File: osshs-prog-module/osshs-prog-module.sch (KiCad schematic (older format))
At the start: 13 parts, among them J1 Conn_02x03_Odd_Even, J2 Conn_01x04, J3 Conn_01x02, SW1 SW_Push, U1 STM32F103RETx

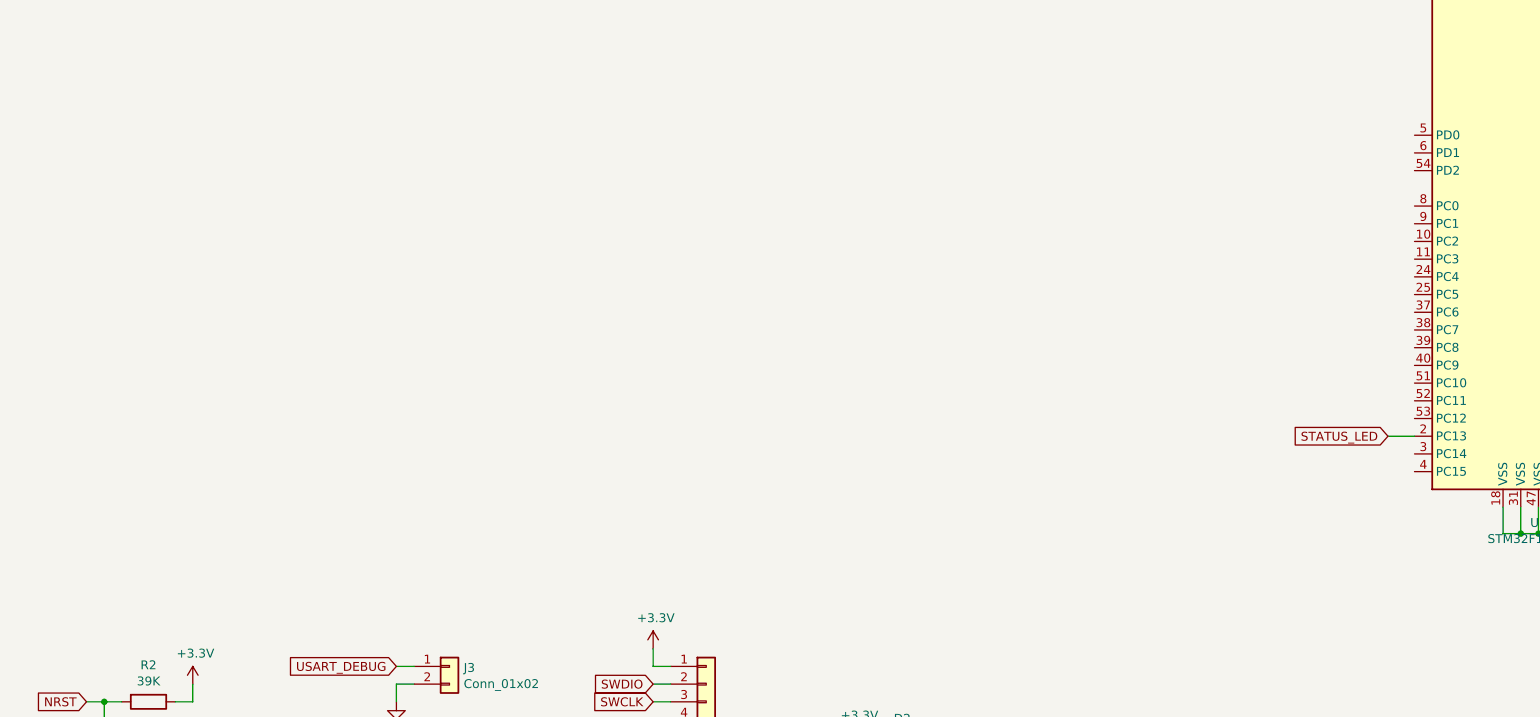
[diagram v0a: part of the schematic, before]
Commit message: Add CAN circuitry
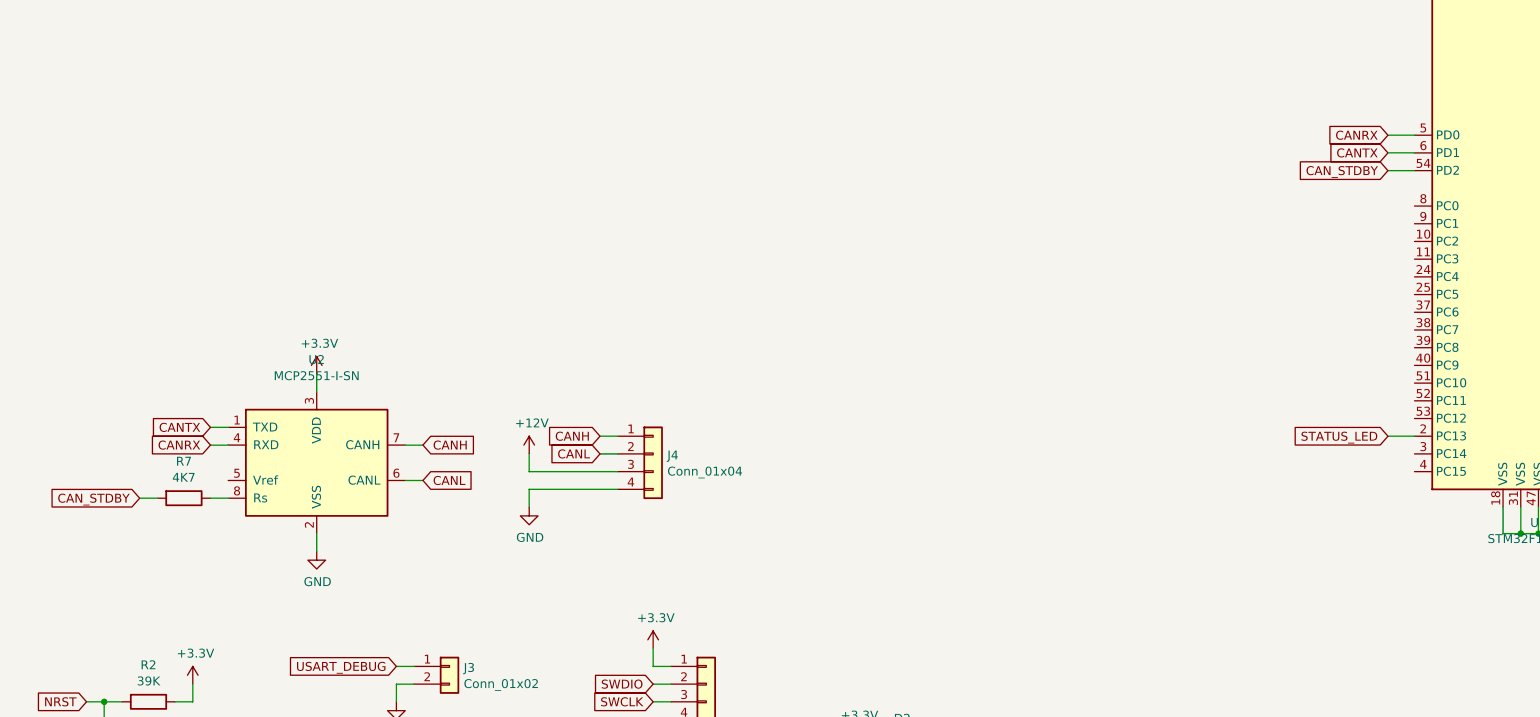
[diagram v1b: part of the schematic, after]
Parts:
- added J4: Conn_01x04, TerminalBlock:TerminalBlock_bornier-4_P5.08mm, symbol Connector_Generic:Conn_01x04
- added R7: 4K7, Resistor_SMD:R_0805_2012Metric, symbol Device:R
- added U2: MCP2551-I-SN, Package_SO:SOIC-8_3.9x4.9mm_P1.27mm, symbol Interface_CAN_LIN:MCP2551-I-SN
- J3: footprint (none) -> Connector_PinHeader_2.54mm:PinHeader_1x02_P2.54mm_Vertical
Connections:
- net +3V3: now also U2.3 (VDD)
- net GND: now also J4.4 (Pin_4), U2.2 (VSS)
- net CANRX: now reaches U1.5 (PD0)
- net CANRX: now also U2.4 (RXD)
- net CAN_STDBY: now reaches U1.54 (PD2)
- net CAN_STDBY: now also R7.2
- net CANTX: now reaches U1.6 (PD1)
- net CANTX: now also U2.1 (TXD)
- new net: R7.1, U2.8 (Rs)
- new net +12V: J4.3 (Pin_3)
- new net CANH: J4.1 (Pin_1), U2.7 (CANH)
- new net CANL: J4.2 (Pin_2), U2.6 (CANL)
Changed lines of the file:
@@
 F 0 "J3" H 2930 6092 50  0000 L CNN
 F 1 "Conn_01x02" H 2930 6001 50  0000 L CNN
-F 2 "" H 2850 6100 50  0001 C CNN
+F 2 "Connector_PinHeader_2.54mm:PinHeader_1x02_P2.54mm_Vertical" H 2850 6100 50  0001 C CNN
 F 3 "~" H 2850 6100 50  0001 C CNN
 	1    2850 6100
@@
 USART_DEBUG
 $Comp
-L power:GND #PWR?
+L power:GND #PWR0113
 U 1 1 5E18289F
 P 2550 6300
-F 0 "#PWR?" H 2550 6050 50  0001 C CNN
+F 0 "#PWR0113" H 2550 6050 50  0001 C CNN
 F 1 "GND" H 2555 6127 50  0000 C CNN
 F 2 "" H 2550 6300 50  0001 C CNN
@@
 Text GLabel 9850 2700 2    50   Input ~ 0
 USART_DEBUG
+$Comp
+L Interface_CAN_LIN:MCP2551-I-SN U2
+U 1 1 5E1DA5F9
+P 2100 4950
+F 0 "U2" H 2100 5531 50  0000 C CNN
+F 1 "MCP2551-I-SN" H 2100 5440 50  0000 C CNN
+F 2 "Package_SO:SOIC-8_3.9x4.9mm_P1.27mm" H 2100 4450 50  0001 C CIN
+F 3 "http://ww1.microchip.com/downloads/en/devicedoc/21667d.pdf" H 2100 4950 50  0001 C CNN
+	1    2100 4950
+	1    0    0    -1
+$EndComp
+Wire Wire Line
+	1600 5150 1500 5150
+$Comp
+L Device:R R7
+U 1 1 5E1E74DD
+P 1350 5150
+F 0 "R7" V 1143 5150 50  0000 C CNN
+F 1 "4K7" V 1234 5150 50  0000 C CNN
+F 2 "Resistor_SMD:R_0805_2012Metric" V 1280 5150 50  0001 C CNN
+F 3 "~" H 1350 5150 50  0001 C CNN
+	1    1350 5150
+	0    1    1    0
+$EndComp
+Wire Wire Line
+	2600 4850 2700 4850
+Wire Wire Line
+	2600 5050 2700 5050
+Text GLabel 2700 4850 2    50   Input ~ 0
+CANH
+Text GLabel 2700 5050 2    50   Input ~ 0
+CANL
+Wire Wire Line
+	2100 4550 2100 4450
+Wire Wire Line
+	2100 5350 2100 5450
+$Comp
+L power:GND #PWR0114
+U 1 1 5E1F498D
+P 2100 5450
+F 0 "#PWR0114" H 2100 5200 50  0001 C CNN
+F 1 "GND" H 2105 5277 50  0000 C CNN
+F 2 "" H 2100 5450 50  0001 C CNN
+F 3 "" H 2100 5450 50  0001 C CNN
+	1    2100 5450
+	1    0    0    -1
+$EndComp
+$Comp
+L power:+3.3V #PWR0115
+U 1 1 5E1F940E
+P 2100 4450
+F 0 "#PWR0115" H 2100 4300 50  0001 C CNN
+F 1 "+3.3V" H 2115 4623 50  0000 C CNN
+F 2 "" H 2100 4450 50  0001 C CNN
+F 3 "" H 2100 4450 50  0001 C CNN
+	1    2100 4450
+	1    0    0    -1
+$EndComp
+Wire Wire Line
+	1600 4750 1500 4750
+Wire Wire Line
+	1600 4850 1500 4850
+Text GLabel 1500 4750 0    50   Input ~ 0
+CANTX
+Text GLabel 1500 4850 0    50   Input ~ 0
+CANRX
+$Comp
+L Connector_Generic:Conn_01x04 J4
+U 1 1 5E20EEC2
+P 4000 4900
+F 0 "J4" H 4080 4892 50  0000 L CNN
+F 1 "Conn_01x04" H 4080 4801 50  0000 L CNN
+F 2 "TerminalBlock:TerminalBlock_bornier-4_P5.08mm" H 4000 4900 50  0001 C CNN
+F 3 "~" H 4000 4900 50  0001 C CNN
+	1    4000 4900
+	1    0    0    -1
+$EndComp
+Wire Wire Line
+	3800 4800 3700 4800
+Wire Wire Line
+	3800 4900 3700 4900
+Text GLabel 3700 4800 0    50   Input ~ 0
+CANH
+Text GLabel 3700 4900 0    50   Input ~ 0
+CANL
+Wire Wire Line
+	3800 5000 3300 5000
+Wire Wire Line
+	3300 5000 3300 4900
+Wire Wire Line
+	3300 5100 3300 5200
+Wire Wire Line
+	3300 5100 3800 5100
+$Comp
+L power:GND #PWR0116
+U 1 1 5E226228
+P 3300 5200
+F 0 "#PWR0116" H 3300 4950 50  0001 C CNN
+F 1 "GND" H 3305 5027 50  0000 C CNN
+F 2 "" H 3300 5200 50  0001 C CNN
+F 3 "" H 3300 5200 50  0001 C CNN
+	1    3300 5200
+	1    0    0    -1
+$EndComp
+$Comp
+L power:+12V #PWR0117
+U 1 1 5E228C10
+P 3300 4900
+F 0 "#PWR0117" H 3300 4750 50  0001 C CNN
+F 1 "+12V" H 3315 5073 50  0000 C CNN
+F 2 "" H 3300 4900 50  0001 C CNN
+F 3 "" H 3300 4900 50  0001 C CNN
+	1    3300 4900
+	1    0    0    -1
+$EndComp
+Wire Wire Line
+	8300 3100 8150 3100
+Text GLabel 8150 3100 0    50   Input ~ 0
+CANRX
+Wire Wire Line
+	8300 3200 8150 3200
+Text GLabel 8150 3200 0    50   Input ~ 0
+CANTX
+Wire Wire Line
+	1200 5150 1100 5150
+Text GLabel 1100 5150 0    50   Input ~ 0
+CAN_STDBY
+Wire Wire Line
+	8300 3300 8150 3300
+Text GLabel 8150 3300 0    50   Input ~ 0
+CAN_STDBY
 $EndSCHEMATC

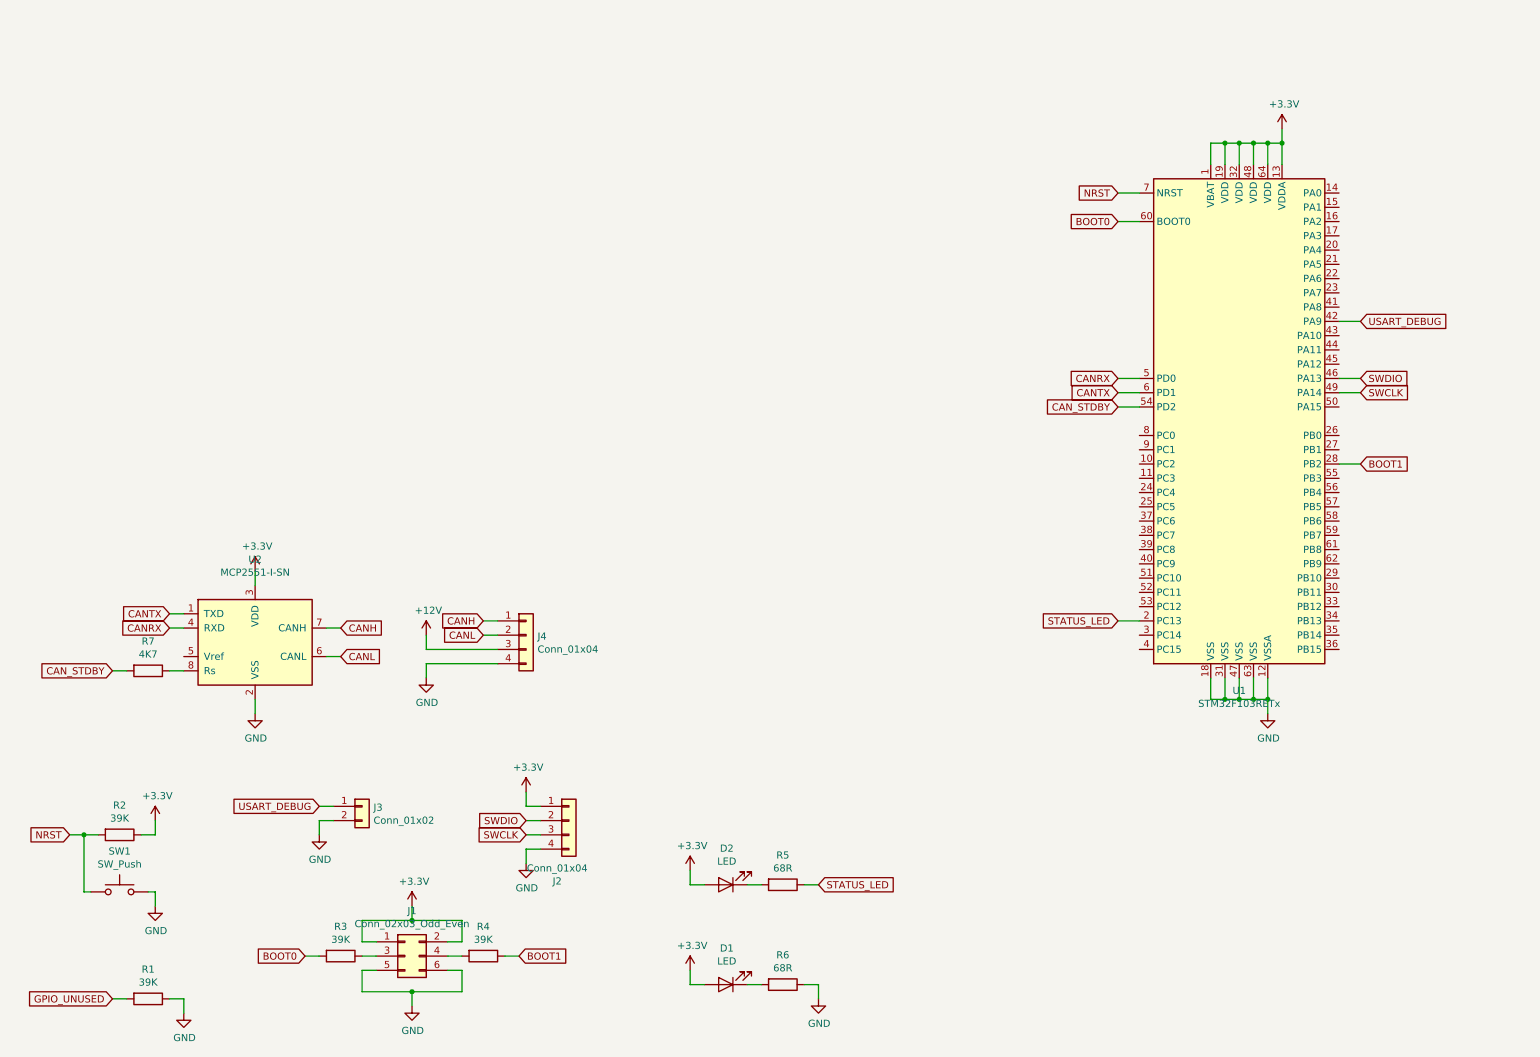
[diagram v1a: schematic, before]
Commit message: Add FT232RL and supporting components
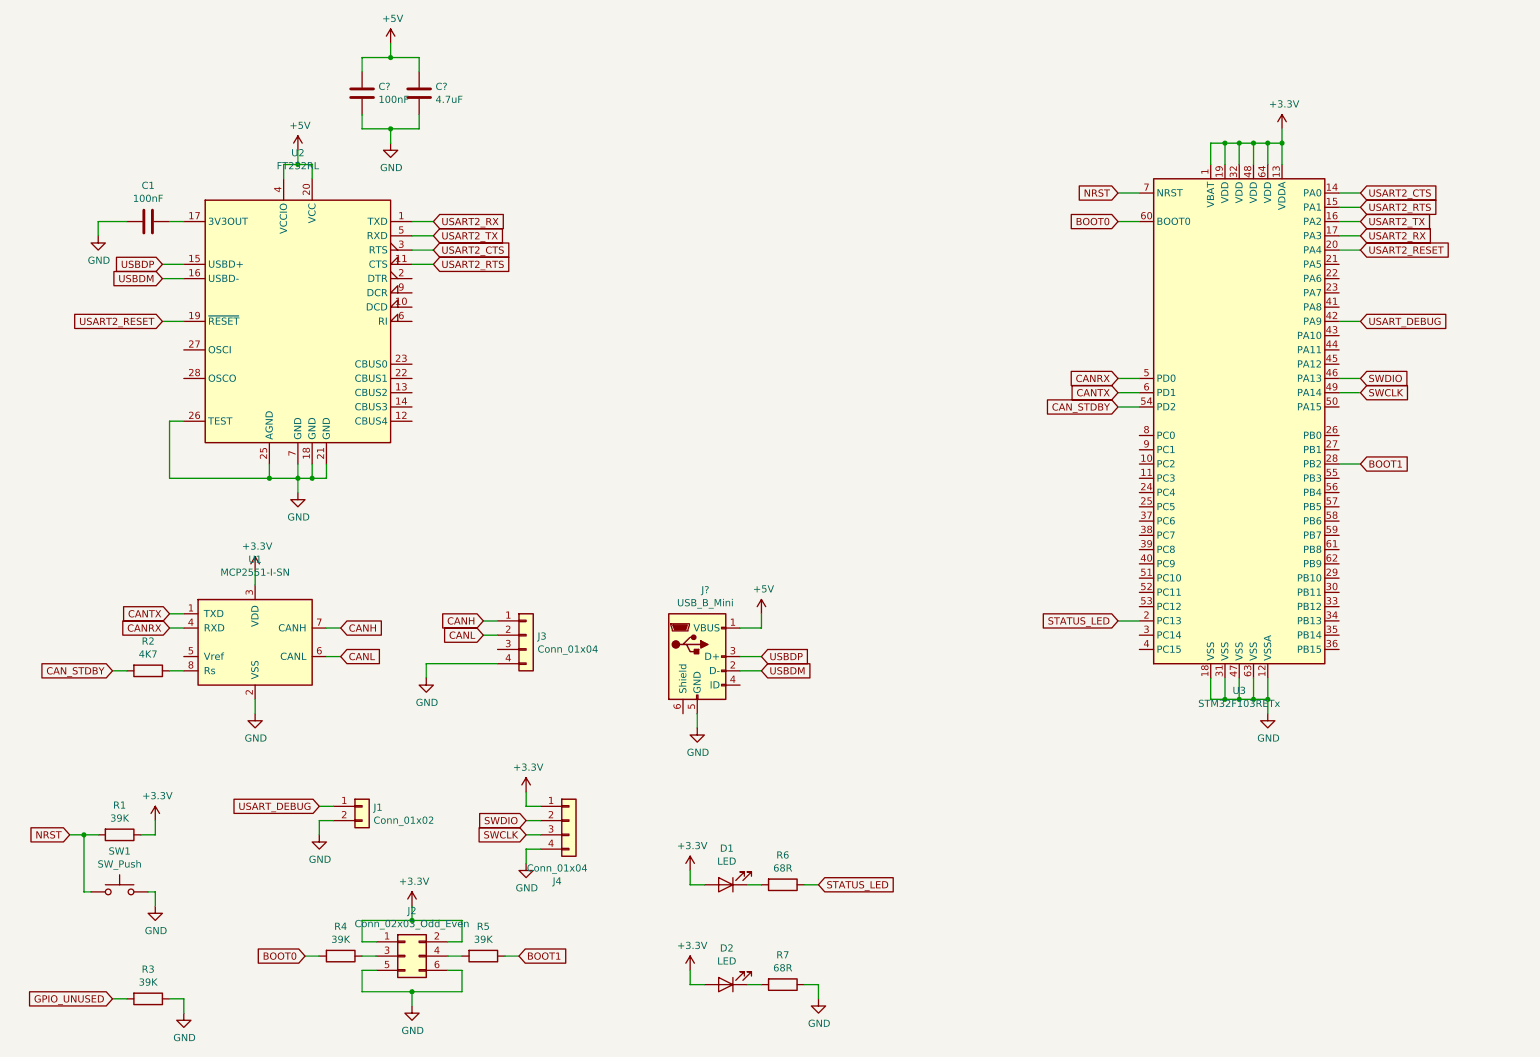
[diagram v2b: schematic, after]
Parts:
- added C1, C?: 100nF, symbol Device:C
- added C?: 4.7uF, symbol Device:C
- added J?: USB_B_Mini, symbol Connector:USB_B_Mini
- added U2: FT232RL, Package_SO:SSOP-28_5.3x10.2mm_P0.65mm, symbol Interface_USB:FT232RL
- renumbered D2 to D1, D1 to D2, J3 to J1, J1 to J2, J4 to J3, J2 to J4, R2 to R1, R7 to R2, R1 to R3, R3 to R4, R4 to R5, R5 to R6, R6 to R7, U2 to U1, U1 to U3
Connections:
- net GND: now also C1.2, C?.1, C?.1, J?.5 (GND), U2.18 (GND), U2.21 (GND), U2.25 (AGND), U2.26 (TEST), U2.7 (GND)
- net USART2_CTS: now reaches U3.14 (PA0)
- net USART2_CTS: now also U2.3 (RTS)
- net USART2_RTS: now reaches U3.15 (PA1)
- net USART2_RTS: now also U2.11 (CTS)
- net USART2_TX: now reaches U3.16 (PA2)
- net USART2_TX: now also U2.5 (RXD)
- net USART2_RX: now reaches U3.17 (PA3)
- net USART2_RX: now also U2.1 (TXD)
- net USART2_RESET: now reaches U3.20 (PA4)
- net USART2_RESET: now also U2.19 (~RESET~)
- net +12V: no longer names the net of J3.3 (Pin_3)
- new net: C1.1, U2.17 (3V3OUT)
- new net +5V: C?.2, C?.2, J?.1 (VBUS), U2.20 (VCC), U2.4 (VCCIO)
- new net USBDM: J?.2 (D-), U2.16 (USBD-)
- new net USBDP: J?.3 (D+), U2.15 (USBD+)

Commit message: Add voltage regulator and decoupling capacitors
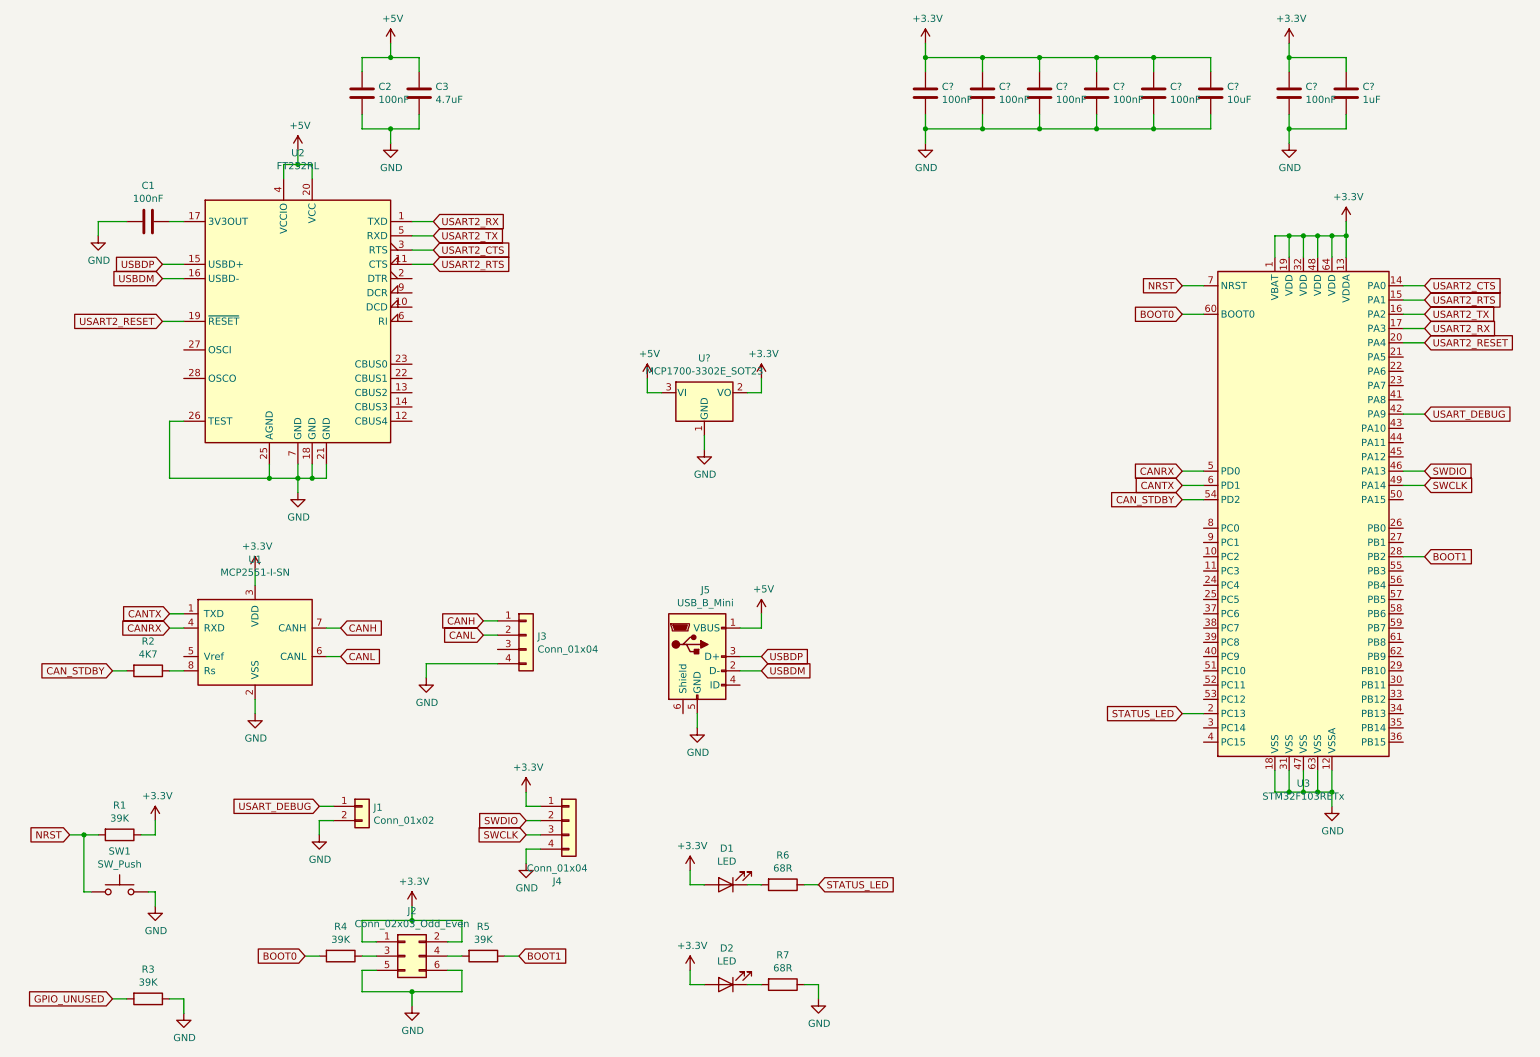
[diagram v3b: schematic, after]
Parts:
- added C? (x6): 100nF, Capacitor_SMD:C_0805_2012Metric, symbol Device:C
- added C?: 10uF, Capacitor_SMD:C_0805_2012Metric, symbol Device:C
- added C?: 1uF, Capacitor_SMD:C_0805_2012Metric, symbol Device:C
- added U?: MCP1700-3302E_SOT23, Package_TO_SOT_SMD:SOT-23, symbol Regulator_Linear:MCP1700-3302E_SOT23
- C1: footprint (none) -> Capacitor_SMD:C_0805_2012Metric
- C2, C3: renamed from C?; footprint (none) -> Capacitor_SMD:C_0805_2012Metric
- J5: renamed from J?; footprint (none) -> Connector_USB:USB_Mini-B_Lumberg_2486_01_Horizontal
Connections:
- net +3V3: now also C?.2, C?.2, C?.2, C?.2, C?.2, C?.2, C?.2, C?.2, U?.2 (VO)
- net +5V: now also U?.3 (VI)
- net GND: now also C?.1, C?.1, C?.1, C?.1, C?.1, C?.1, C?.1, C?.1, U?.1 (GND)
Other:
- moved on the sheet: U3
